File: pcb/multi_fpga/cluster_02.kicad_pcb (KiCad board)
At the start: 2 copper layers, 208.8 x 161.3 mm, 52 parts, among them U49 Comment, U50 Comment, U51 Comment, U52 Comment, U53 Comment, U54 Comment, U55 Comment, U56 Comment, U57 Comment, U58 Comment, U59 Comment, U60 Comment, U61 Comment, U62 Comment, U63 Comment, U64 Comment, U65 Comment, U66 Comment, U67 Comment, U68 Comment, U69 Comment, U70 Comment, U71 Comment, U72 Comment

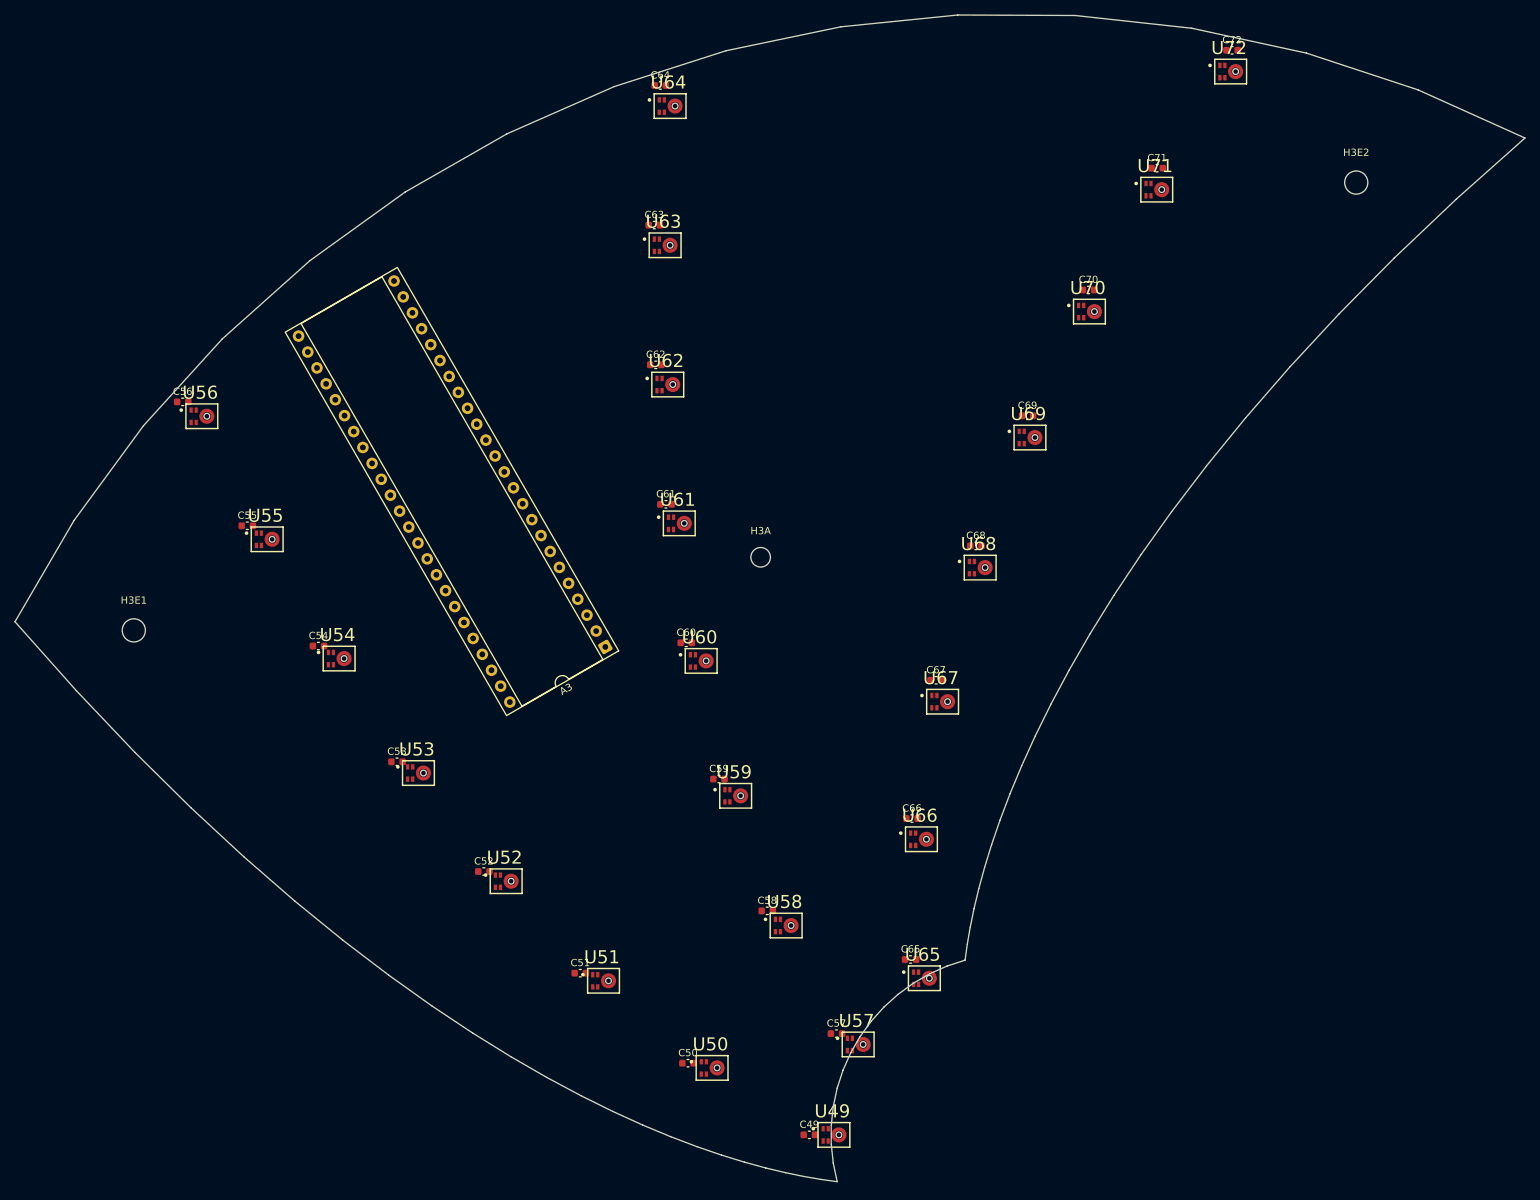
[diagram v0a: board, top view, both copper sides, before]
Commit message: Fixed inner circle of mics.
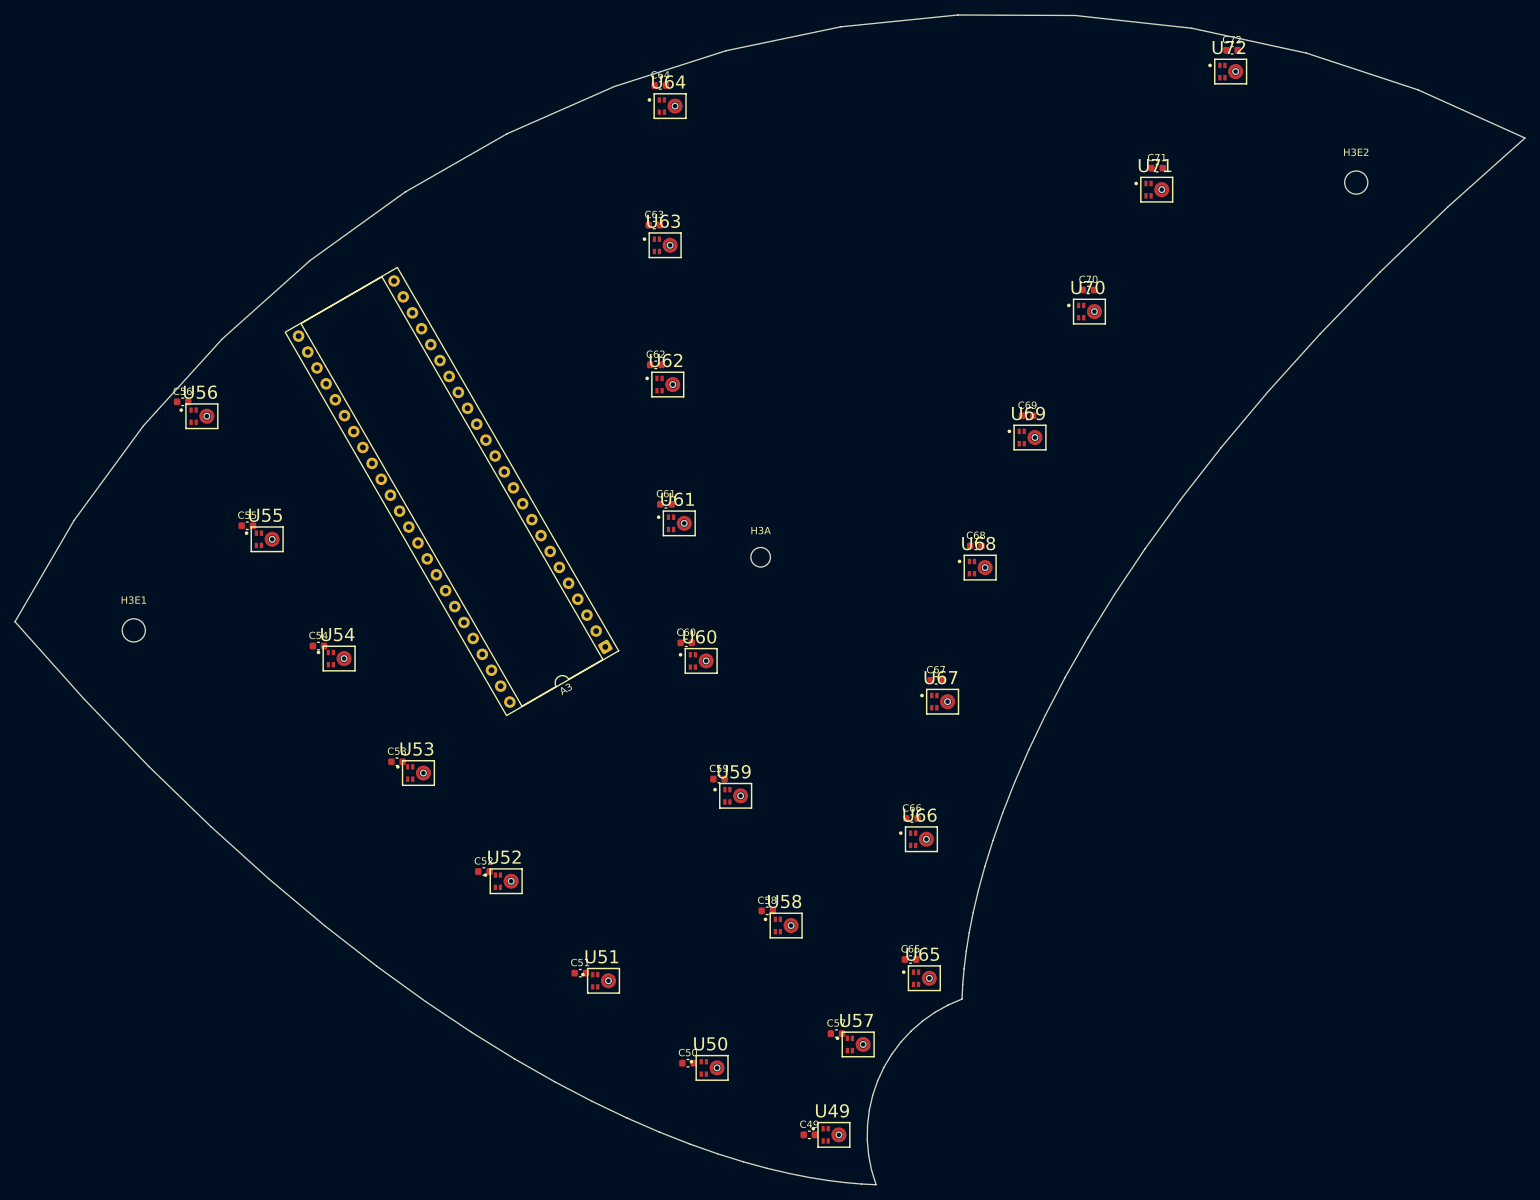
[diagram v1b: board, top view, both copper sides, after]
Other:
- board size 208.8 x 161.3 mm -> 208.8 x 161.7 mm
